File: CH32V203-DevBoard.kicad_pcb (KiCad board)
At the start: 2 copper layers, 20.3 x 50.8 mm, 44 parts, among them J1 USB_C_Receptacle_USB2.0_16P, J2 USB_C_Receptacle_USB2.0_16P, Q1 AO3401A, Q2 AO3401A, SW1 SW_Push, SW2 SW_Push, U1 CH32V203C8T6, U2 RT9080-33GJ5

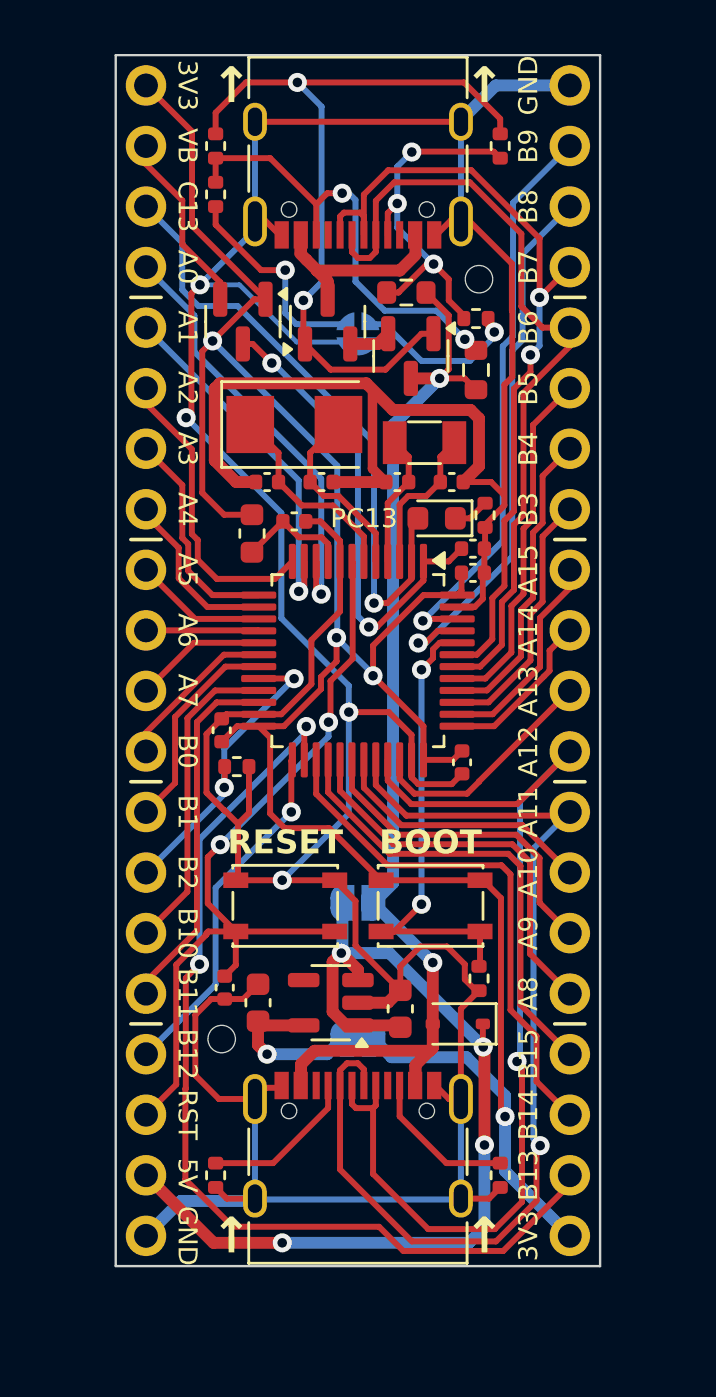
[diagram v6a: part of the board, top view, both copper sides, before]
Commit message: fix wire width
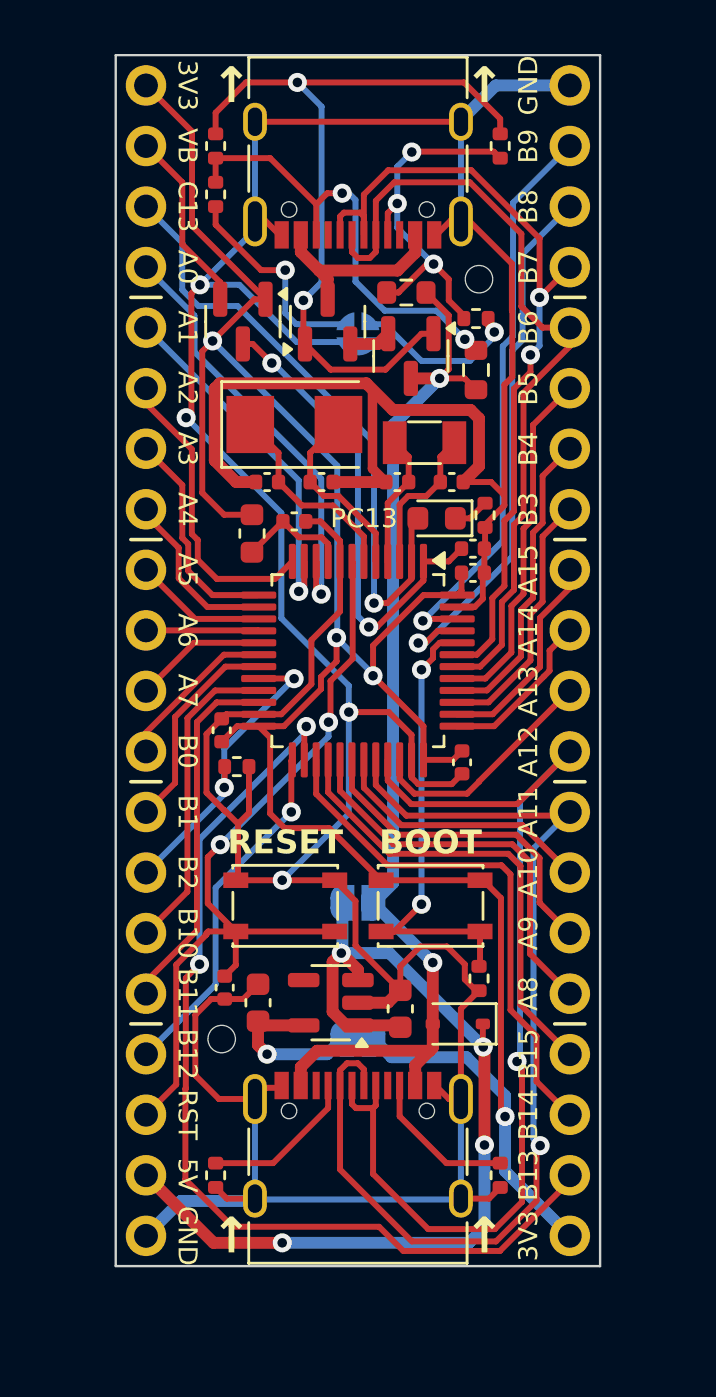
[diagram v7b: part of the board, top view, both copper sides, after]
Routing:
- net Net-(Q2-D): track 7.08 -> 8.54 mm
- net VBUS: track 45.1 -> 45.9 mm
